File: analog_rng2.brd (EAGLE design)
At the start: 54 x 44.8 mm, 63 parts, among them IC2 LM2903D, IC3 OPA4134D, U1 TLV73325, U2 TPS70925, U23423 LM277625

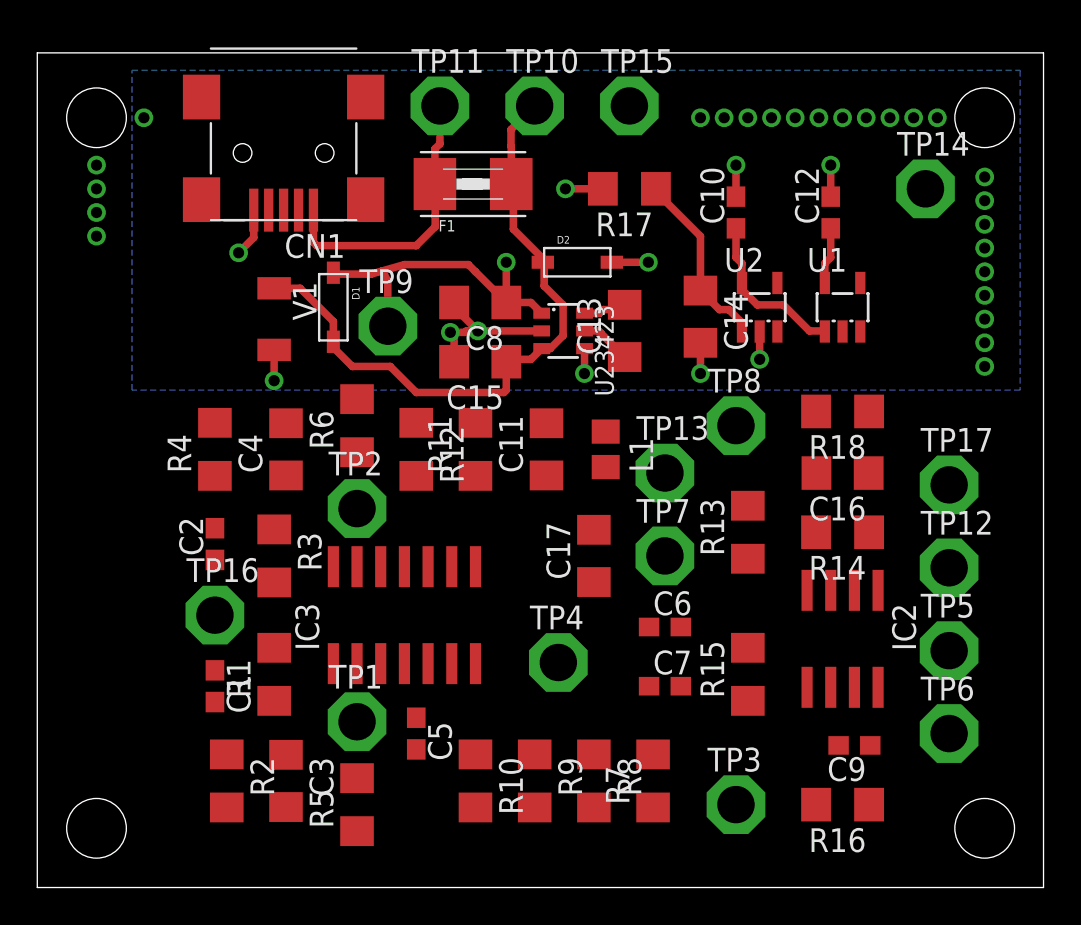
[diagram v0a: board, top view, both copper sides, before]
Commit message: More layout work done, finished first cut at copper layout
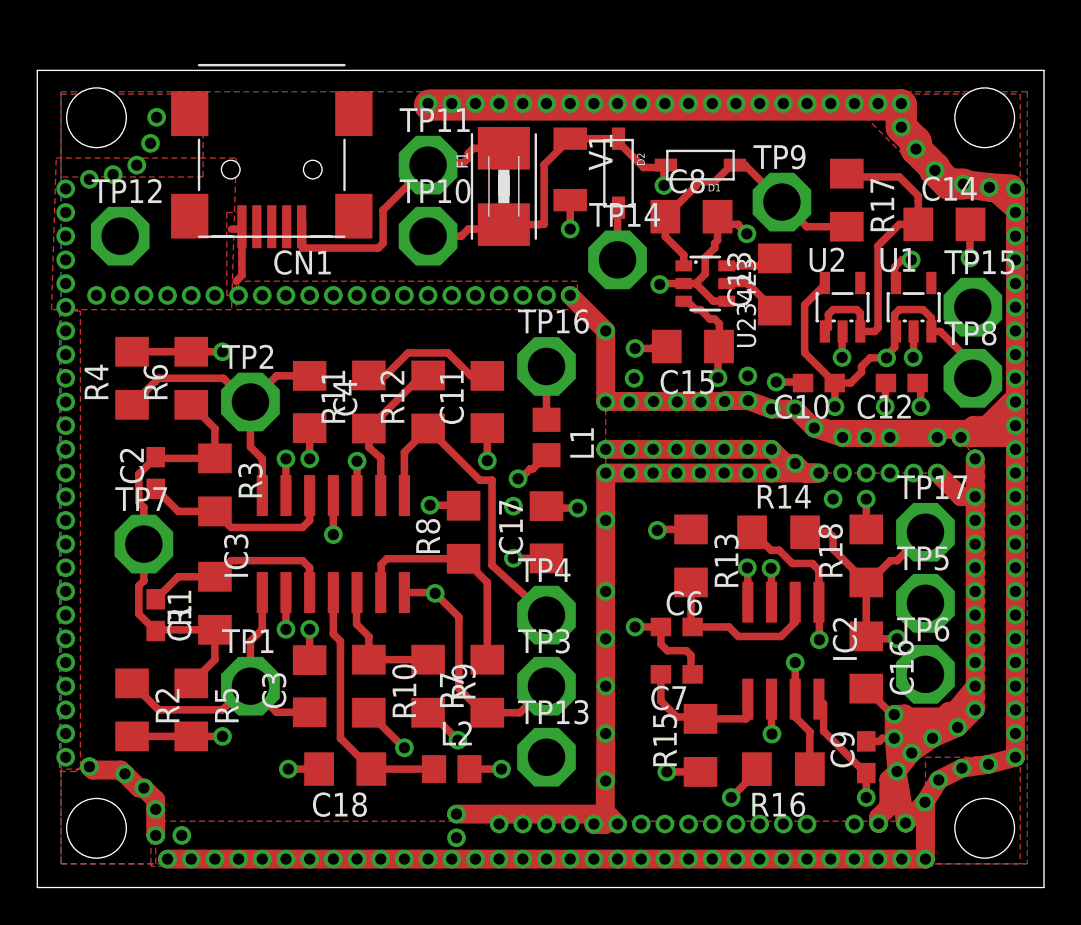
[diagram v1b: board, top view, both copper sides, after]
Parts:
- removed C5: 0.1uF, vreg_local:C0603
- added C18: 10uF, vreg_local:C1206
- added L2: BLM18BB600SN1D, vreg_local:R0805
- moved TP12 47.9 mm to (4.45, 34.9)
- moved TP7 27.9 mm to (5.71, 18.4)
- moved TP16 22.2 mm to (27.3, 27.9)
- moved TP9 22.2 mm to (39.9, 36.8)
- moved TP15 21.3 mm to (50.2, 31.1)
- moved D1 21.1 mm to (35.6, 38.7), turned to 180 degrees
- moved V1 17.8 mm to (28.6, 38.5)
- moved TP14 16.9 mm to (31.1, 33.7)
- moved TP13 16.5 mm to (27.3, 6.99)
- moved R8 15.1 mm to (22.9, 19.1), turned to 90 degrees
- moved C14 14.0 mm to (48.6, 35.6), turned to 0 degrees
- moved TP8 13.0 mm to (50.2, 27.3)
- moved C8 12.2 mm to (35.1, 36.0), turned to 0 degrees
- moved TP3 12.0 mm to (27.3, 10.8)
- moved R17 11.7 mm to (43.4, 36.9), turned to 270 degrees
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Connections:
- new net P5VP: C18.1, IC3.4, L2.1
- net P5V: now also L2.2; no longer C5.1, IC3.4
- net PE: now also C18.2; no longer C5.2
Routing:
- net PE: track 22.7 -> 892.3 mm, vias 9 -> 242
- net P5V: track 8.79 -> 92.8 mm, vias 0 -> 5
- net P2R5VF: track 0.00 -> 38.7 mm, vias 0 -> 8
- net P2R5V: track 3.06 -> 40.1 mm, vias 0 -> 2
- net P5VD: track 0.00 -> 31.7 mm, vias 0 -> 2
- net RNDAMP: track 0.00 -> 27.5 mm, vias 0 -> 1
- net RNDLLDC: track 0.00 -> 24.2 mm, vias 0 -> 2
- net V1DC: track 0.00 -> 16.5 mm
- net V2DC: track 0.00 -> 16.5 mm
- net VPP2F: track 0.00 -> 15.2 mm, vias 0 -> 2
- net VPP1F: track 0.00 -> 15.2 mm, vias 0 -> 2
- net RNDP: track 0.00 -> 14.7 mm, vias 0 -> 1
- net P5VP: track 0.00 -> 13.7 mm
- net RNDN: track 0.00 -> 13.3 mm, vias 0 -> 1
- net V1: track 0.00 -> 13.1 mm, vias 0 -> 2
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- added copper zone on layer 2, net P2R5VF
- added copper zone on layer 1, net PE
- added copper zone on layer 15, net PE
- added copper zone on layer 2, net PE
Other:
- board size 54 x 44.8 mm -> 54 x 43.8 mm
